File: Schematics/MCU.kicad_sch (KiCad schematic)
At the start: 31 parts, among them J1 Microsemi_FlashPro-JTAG-10, Q3 BC817, SW1 SAMZO G4R0015010, SW2 SAMZO G4R0015010, U1 STM32F405RGT6, Y1 8mhz

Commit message: reviewed schematic and pcb and replaced part numbers, added and named datasheets into document folder
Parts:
- D1: LCSC C114586 -> C2761795
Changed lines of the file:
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@@
 			)
 		)
-		(property "LCSC" "C114586"
+		(property "LCSC" "C2761795"
 			(at 17.018 183.134 0)
 			(effects

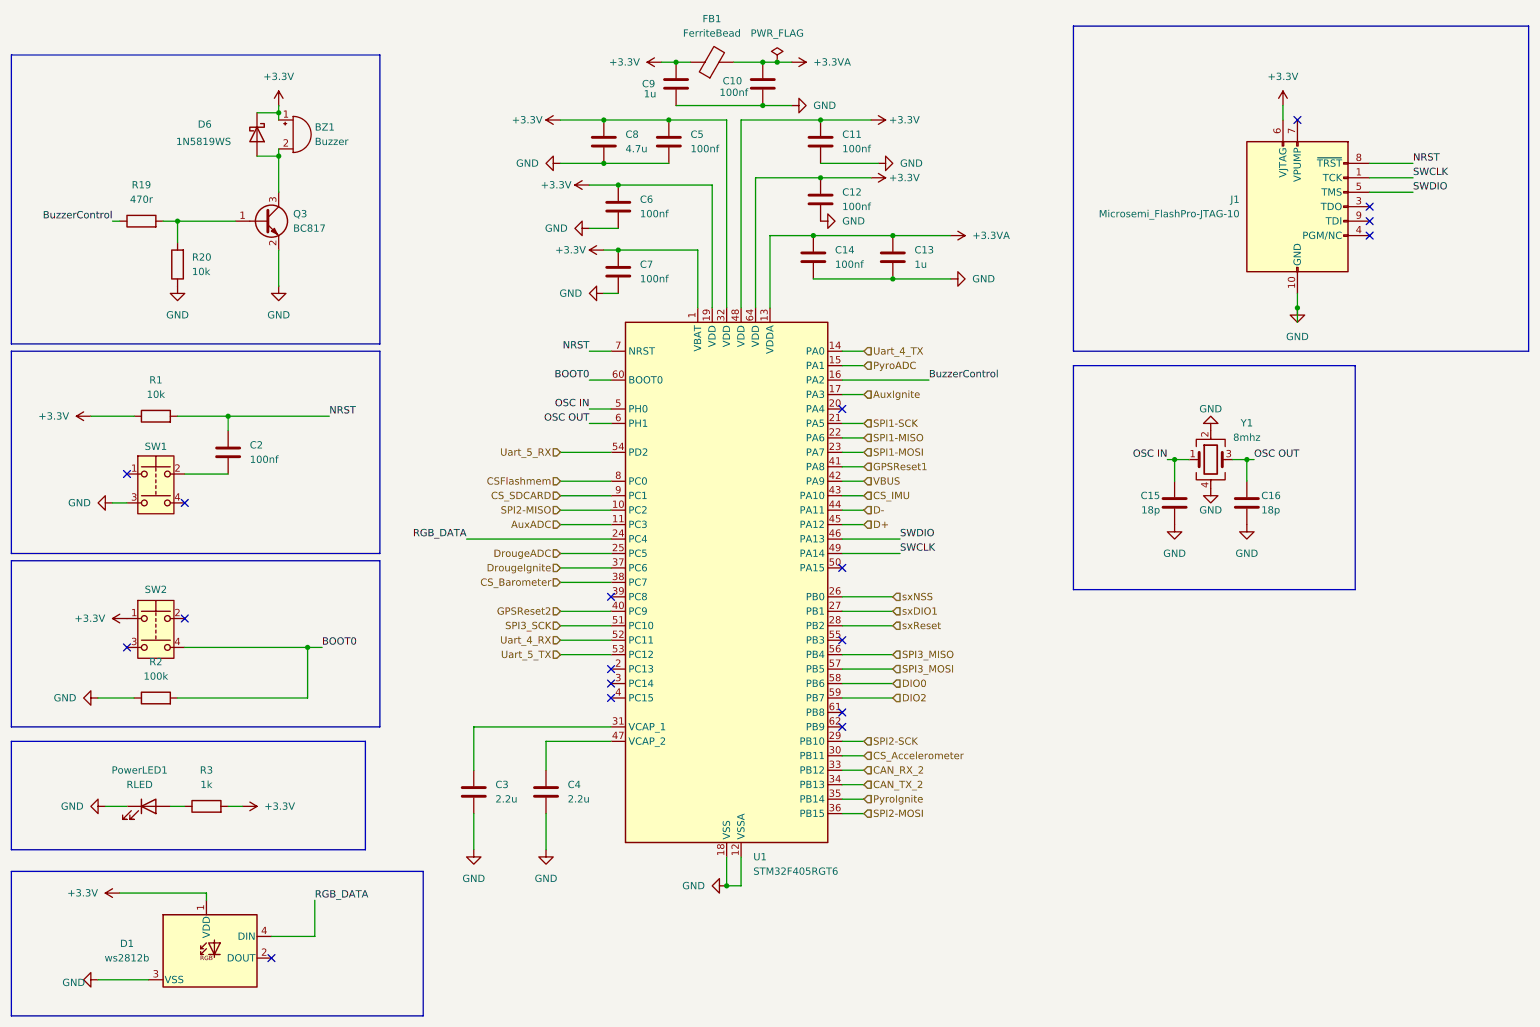
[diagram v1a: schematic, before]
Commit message: updated to KiCad 10.0, updated .gitignore
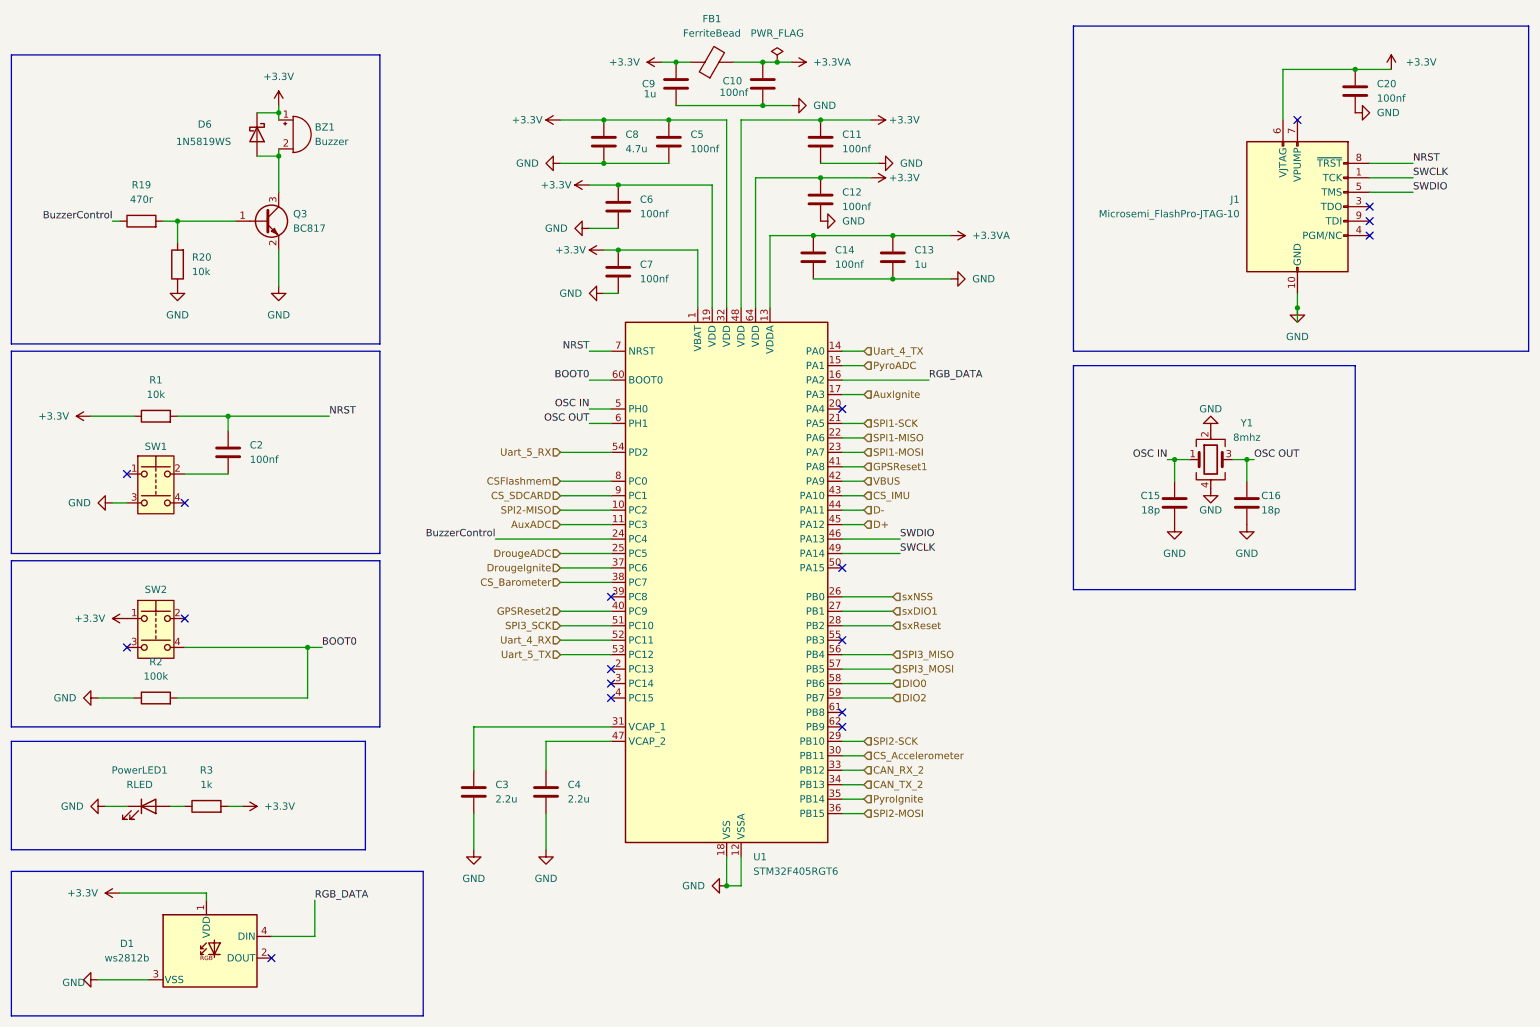
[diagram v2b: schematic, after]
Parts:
- added C20: 100nf, Capacitor_SMD:C_0805_2012Metric_Pad1.18x1.45mm_HandSolder, symbol Device:C
- C3, C4: LCSC C19110 -> C377773
- FB1: LCSC C85840 -> C1015
- J1: now left out of the parts list
- R1, R20: LCSC C84376 -> C17414
- R19: LCSC C2907267 -> C17710
- R2: LCSC C96346 -> C149504
- R3: LCSC C95781 -> C17513
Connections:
- net +3.3V: now also C20.1
- net BuzzerControl: now also U1.24 (PC4); no longer U1.16 (PA2)
- net GND: now also C20.2
- net RGB_DATA: now also U1.16 (PA2); no longer U1.24 (PC4)

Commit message: updated stlink
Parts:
- J1: footprint myFootprints:CONN_7024610XX_MOL -> Connector_PinHeader_1.27mm:PinHeader_2x05_P1.27mm_Vertical; LCSC C588426 -> C22438120

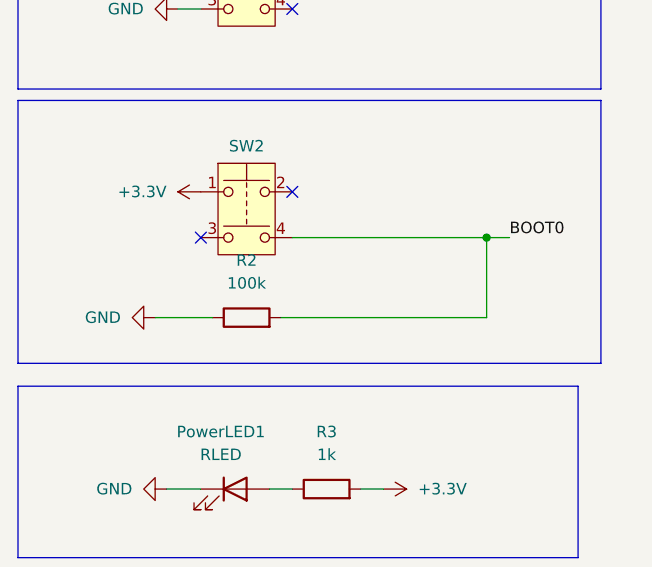
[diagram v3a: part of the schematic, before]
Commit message: updated Schematic for final order
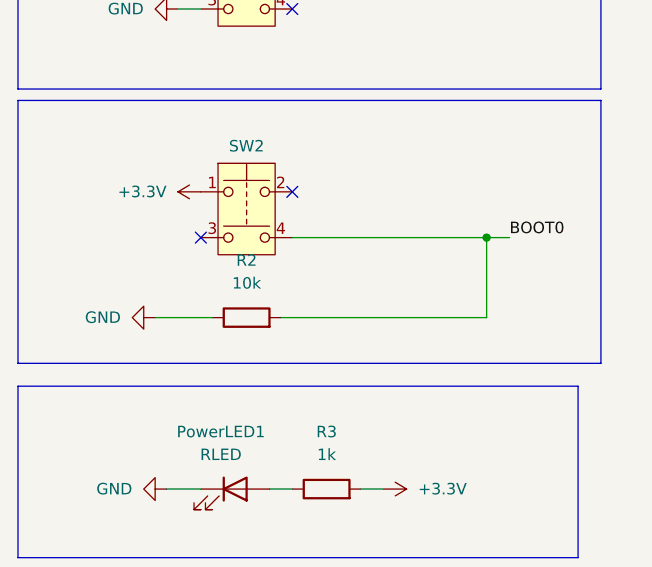
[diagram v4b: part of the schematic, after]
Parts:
- R2: value 100k -> 10k
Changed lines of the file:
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@@
 			)
 		)
-		(property "Value" "100k"
+		(property "Value" "10k"
 			(at 40.64 134.62 90)
 			(show_name no)

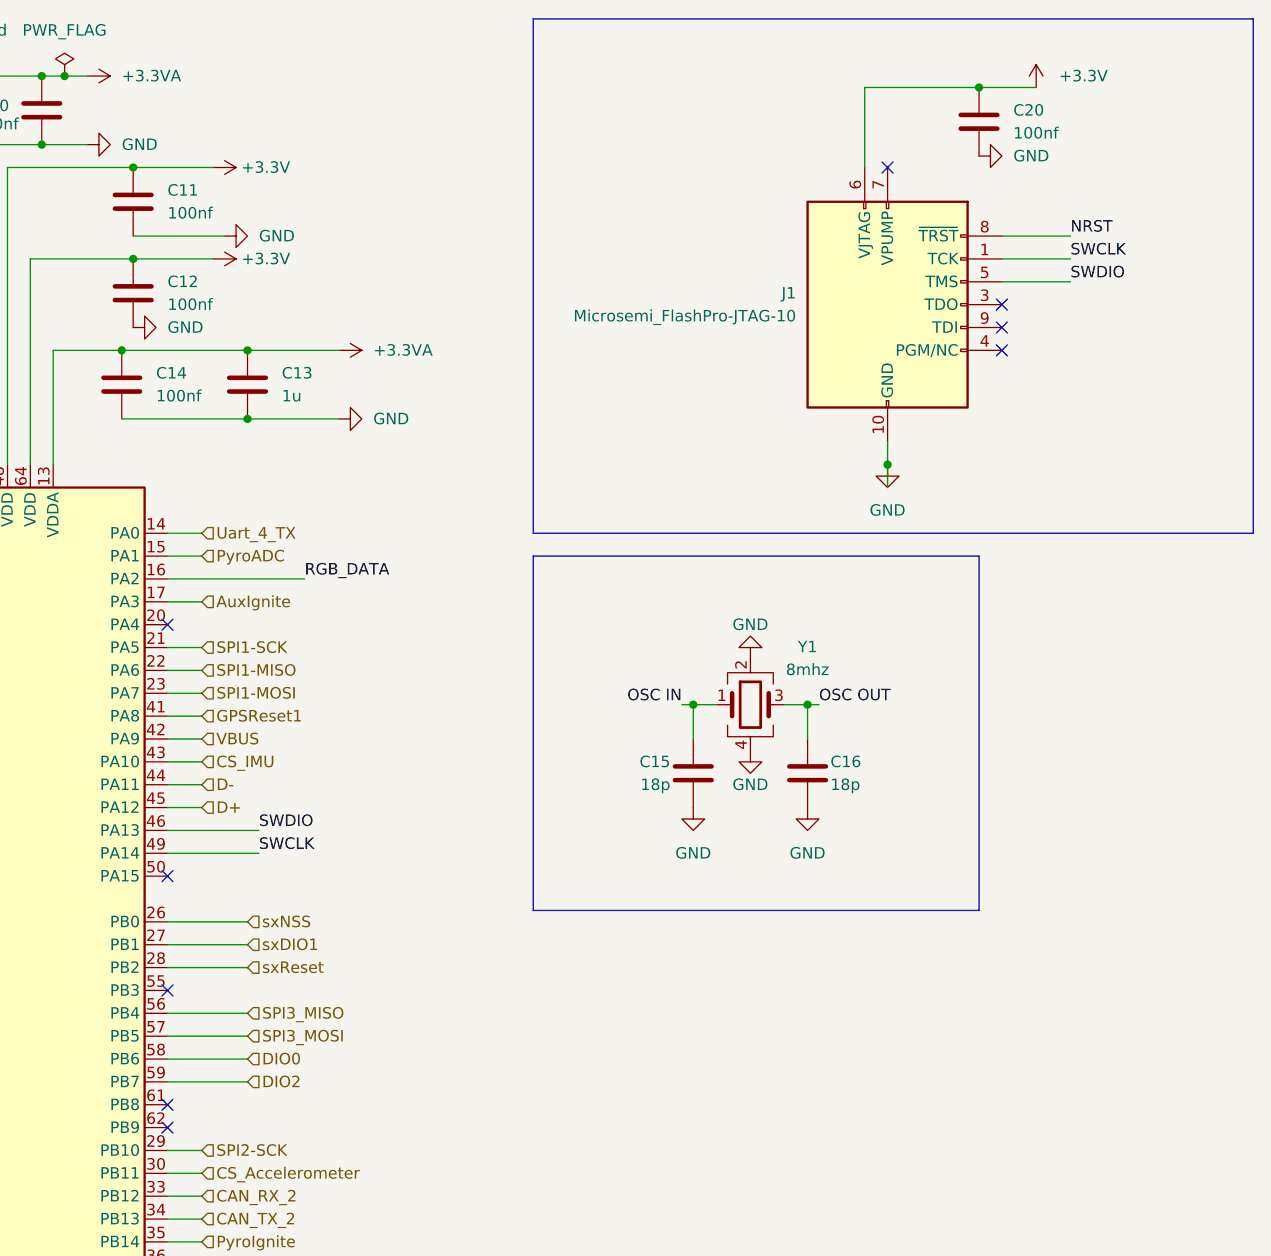
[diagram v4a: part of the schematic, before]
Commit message: fixed STLINK connector with correct pin mapping
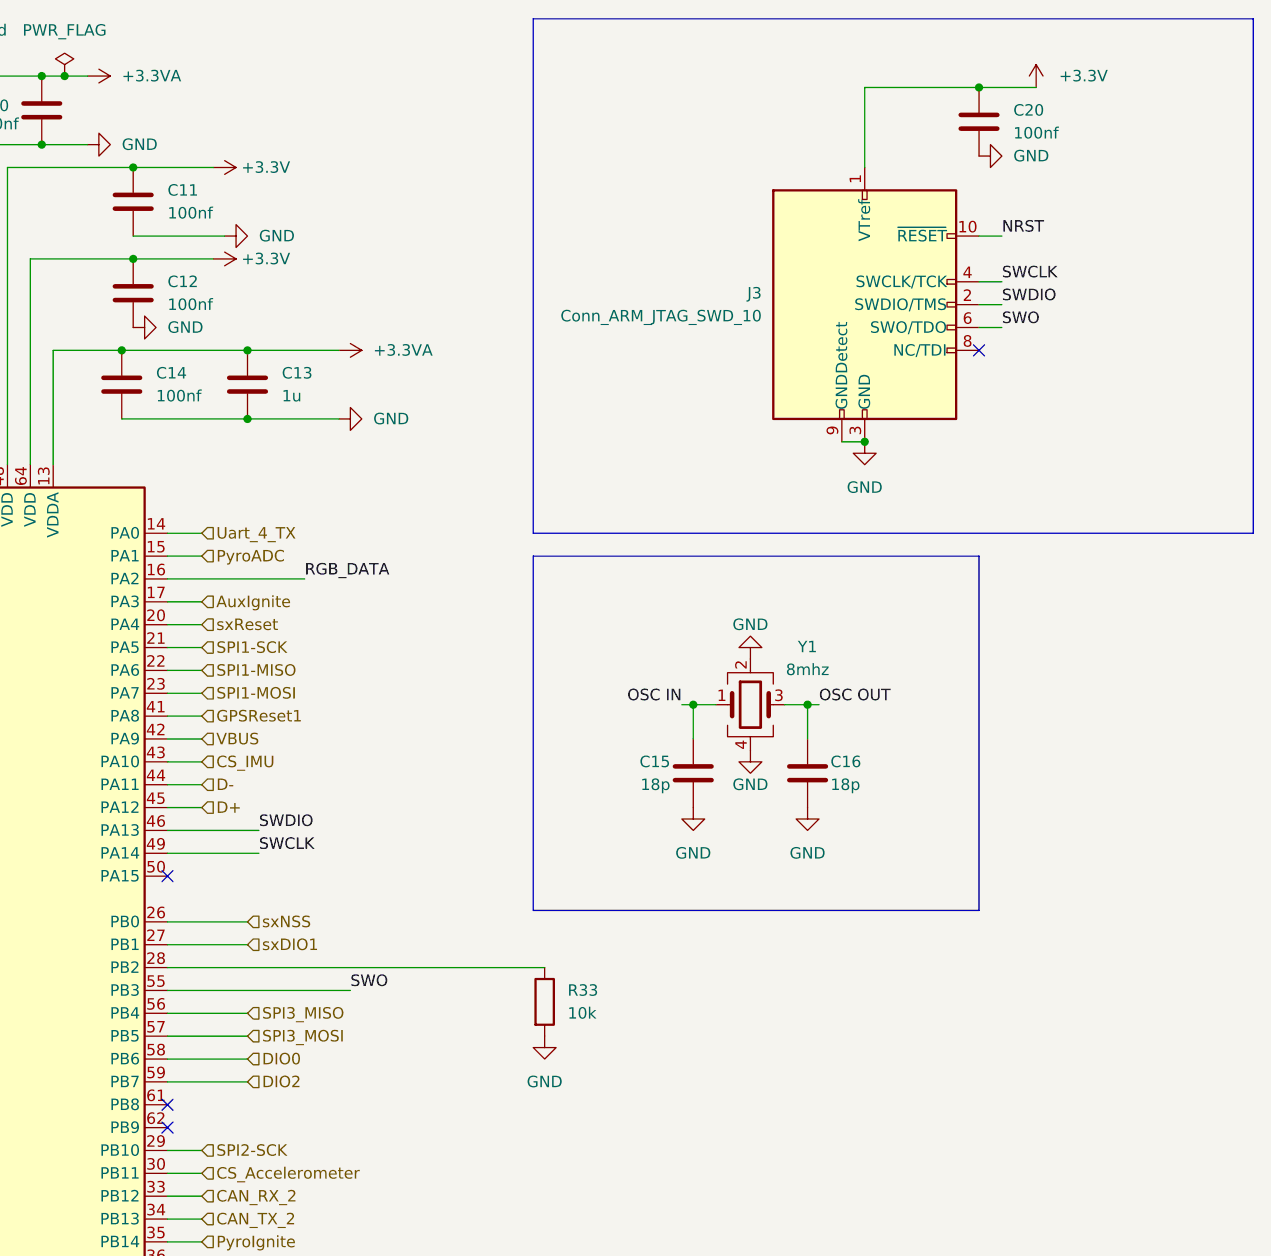
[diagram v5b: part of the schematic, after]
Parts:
- removed J1: Microsemi_FlashPro-JTAG-10, Connector_PinHeader_1.27mm:PinHeader_2x05_P1.27mm_Vertical, symbol Connector:Microsemi_FlashPro-JTAG-10
- added J3: Conn_ARM_JTAG_SWD_10, Connector_PinHeader_1.27mm:PinHeader_2x05_P1.27mm_Vertical, symbol Custom1:Conn_ARM_JTAG_SWD_10
- added R33: 10k, Resistor_SMD:R_0805_2012Metric, symbol Device:R
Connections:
- net +3.3V: now also J3.1 (VTref)
- net GND: now also J3.3 (GND), J3.5 (GND), J3.9 (GNDDetect), R33.2
- net NRST: now also J3.10 (~{RESET})
- net SWCLK: now also J3.4 (SWCLK/TCK)
- net SWDIO: now also J3.2 (SWDIO/TMS)
- net sxReset: now also U1.20 (PA4); no longer U1.28 (PB2)
- net SWO: now reaches U1.55 (PB3)
- net SWO: now also J3.6 (SWO/TDO)
- new net: R33.1, U1.28 (PB2)
- no-connect marks 18 -> 13
